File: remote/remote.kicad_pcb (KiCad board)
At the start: 2 copper layers, 26 parts, among them IC1 ATMEGA328P-A, P5 HD44780_LCD, P6 CONN_02X03, Q1 BC349, Q2 BC349, Q3 BC358, Q4 BC358, Q5 BC358

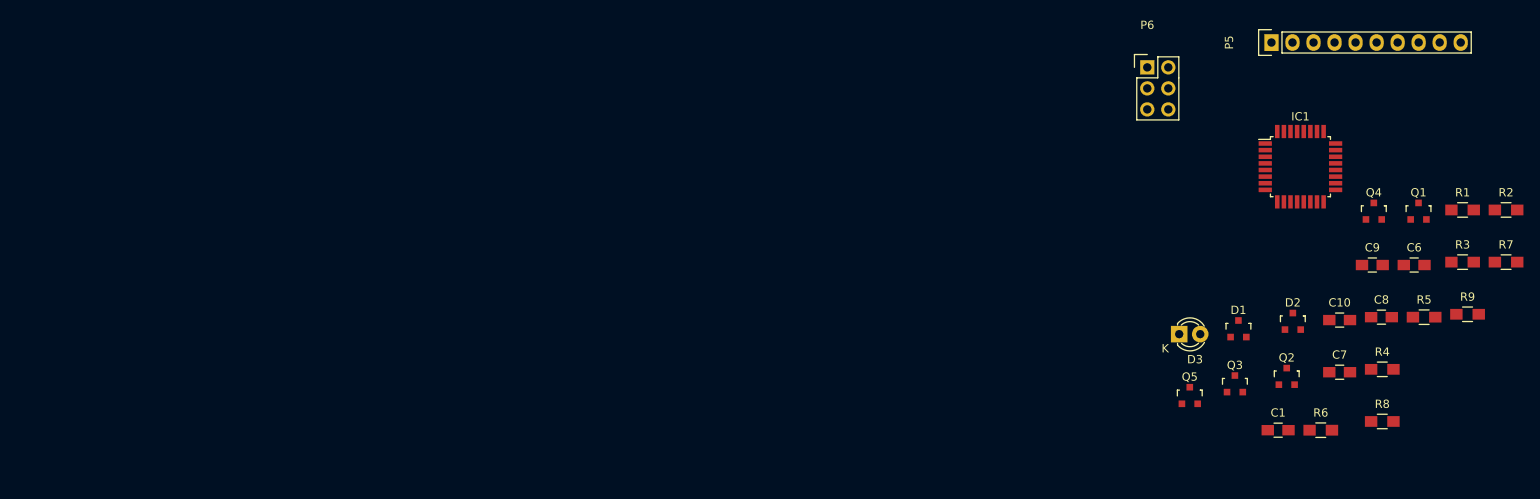
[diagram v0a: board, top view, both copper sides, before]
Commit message: finished layouting the collector unit
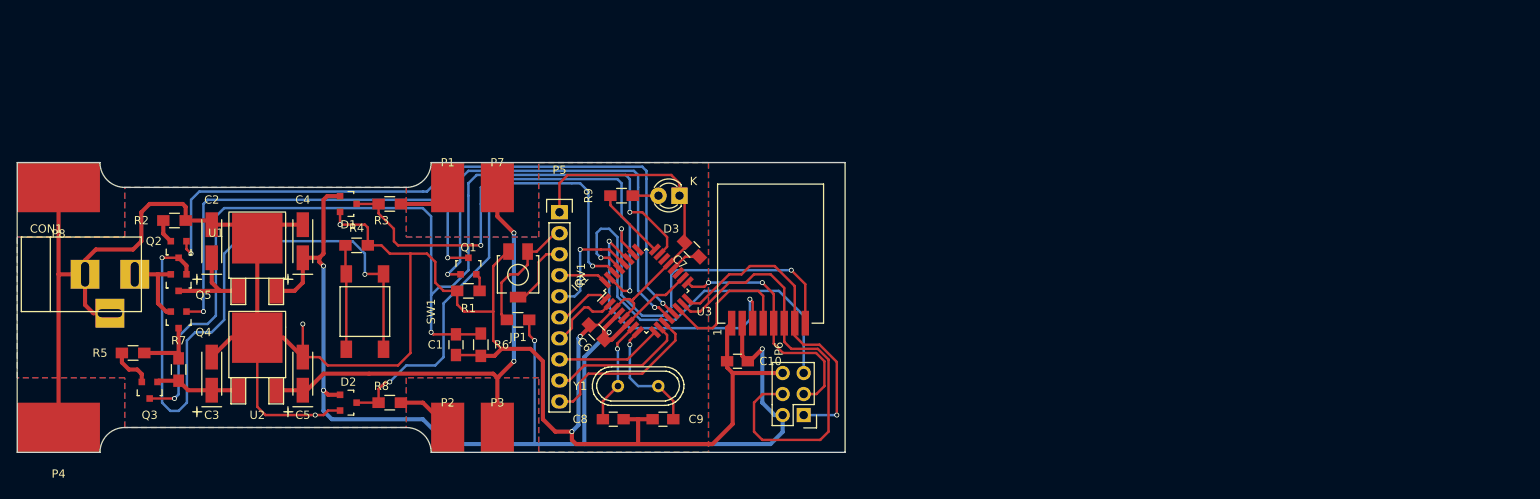
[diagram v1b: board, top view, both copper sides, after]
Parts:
- added C2: 1u, Capacitors_Tantalum_SMD:TantalC_SizeA_EIA-3216_HandSoldering, F.Cu at (75.5, 97.5)
- added C3: 1u, Capacitors_Tantalum_SMD:TantalC_SizeA_EIA-3216_HandSoldering, F.Cu at (75.5, 113.5)
- added C4: 1u, Capacitors_Tantalum_SMD:TantalC_SizeA_EIA-3216_HandSoldering, F.Cu at (86.5, 97.5)
- added C5: 1u, Capacitors_Tantalum_SMD:TantalC_SizeA_EIA-3216_HandSoldering, F.Cu at (86.5, 113.5)
- added CON1: BARREL_JACK, Connect:BARREL_JACK, F.Cu at (60.0, 101.5)
- added JP1: JUMPER, Resistors_SMD:R_0805_HandSoldering, F.Cu at (112.5, 107.0)
- added P1: CON_TX, custom:SmallFoilCon, F.Cu at (104.0, 91.0)
- added P2: CON_RX, custom:SmallFoilCon, F.Cu at (104.0, 120.0)
- added P3: BRICK_P, custom:SmallFoilCon, F.Cu at (110.0, 120.0)
- added P4: BRICK_N, custom:BigFoilCon, F.Cu at (57.0, 120.0)
- added P7: BRICK_P, custom:SmallFoilCon, F.Cu at (110.0, 91.0)
- added P8: BRICK_N, custom:BigFoilCon, F.Cu at (57.0, 91.0)
- added RV1: POT, custom:Cermet_Model23, F.Cu at (112.5, 101.5)
- added SW1: SEND, custom:Schurter_LSG_1301, F.Cu at (94.0, 106.0)
- added U1: TS2940 CP33, TO_SOT_Packages_SMD:TO-252-2Lead, F.Cu at (81.0, 103.5)
- added U2: TS2940 CP33, TO_SOT_Packages_SMD:TO-252-2Lead, F.Cu at (81.0, 115.5)
- added U3: RFM75, custom:RFM75, F.Cu at (143.0, 99.0)
- added Y1: 12MHz, Crystals:Crystal_HC49-U_Vertical, F.Cu at (127.0, 115.0)
- moved R7 160.9 mm to (71.5, 113.0), turned to 270 degrees
- moved R2 160.8 mm to (71.0, 95.0)
- moved R5 156.0 mm to (66.0, 111.0)
- moved Q4 145.0 mm to (71.5, 107.0), turned to 180 degrees
- moved Q2 134.7 mm to (71.5, 98.5), turned to 180 degrees
- moved Q3 131.1 mm to (68.0, 115.5), turned to 180 degrees
- moved R3 129.8 mm to (97.0, 93.0)
- moved R4 124.8 mm to (93.0, 98.0)
- moved Q5 122.9 mm to (71.5, 102.5), turned to 180 degrees
- moved R1 120.5 mm to (106.5, 103.5), turned to 180 degrees
- moved R8 119.9 mm to (97.0, 117.0)
- moved Q1 115.0 mm to (106.5, 100.5)
- moved D2 114.5 mm to (92.0, 117.0), turned to 270 degrees
- moved D1 108.6 mm to (92.0, 93.0), turned to 270 degrees
- moved R9 103.2 mm to (125.0, 92.0), turned to 180 degrees
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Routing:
- net GND: track 0.00 -> 319.9 mm, vias 0 -> 5
- net +3V3: track 0.00 -> 163.9 mm, vias 0 -> 5
- net /BRICK_I_FB: track 0.00 -> 123.9 mm, vias 0 -> 3
- net /UC_ON: track 0.00 -> 84.6 mm, vias 0 -> 2
- net Net-(Q2-Pad3): track 0.00 -> 78.9 mm, vias 0 -> 2
- net /UART_RX: track 0.00 -> 61.1 mm, vias 0 -> 2
- net /UART_TX: track 0.00 -> 59.7 mm, vias 0 -> 2
- net Net-(C5-Pad1): track 0.00 -> 58.4 mm, vias 0 -> 2
- net /BRICK_ON: track 0.00 -> 54.9 mm, vias 0 -> 2
- net /MOSI: track 0.00 -> 53.8 mm
- net Net-(Q1-Pad3): track 0.00 -> 53.7 mm, vias 0 -> 2
- net /~RESET: track 0.00 -> 49.6 mm, vias 0 -> 1
- net /RFM_IRQ: track 0.00 -> 44.9 mm, vias 0 -> 2
- net /MISO: track 0.00 -> 38.8 mm, vias 0 -> 1
- net /RFM_CE: track 0.00 -> 35.2 mm, vias 0 -> 2
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- added copper zone on B.Cu, net GND
- added copper zone on F.Cu, net GND
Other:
- board outline added: 100 x 35 mm
- net class Default: trace_width 0.25 -> 0.3
- board text added: "Collector zerforscht.de"
